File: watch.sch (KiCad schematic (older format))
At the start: 16 parts, among them IC1 ATMEGA48A-M

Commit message: Are finished yet? I think we are...
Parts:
- removed C? (x2): C, symbol C
- added C1, C2, C3, C4: C, symbol C
- added R1, R2, R3: R, symbol R
- gave numbers to parts that had none: 1
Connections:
- net labels added: LED01, LED02, LED03, LED04, LED05, LED06, LED07, LED08, LED09, LED10, LED11, LED12, MISO, MOSI, RESET, SCK, VCC
- wire segments 67 -> 109

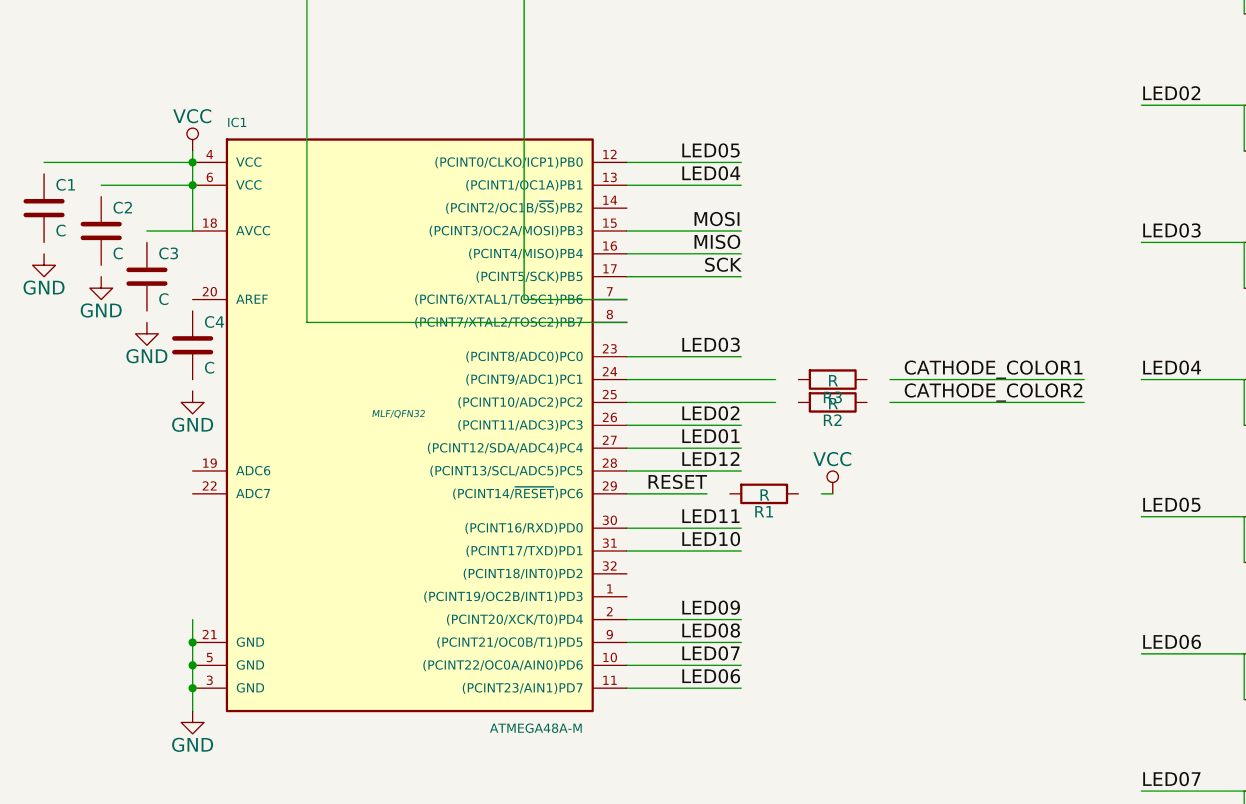
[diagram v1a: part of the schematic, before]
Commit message: Stupid kicad library update broke the schematics. Duhgit add .
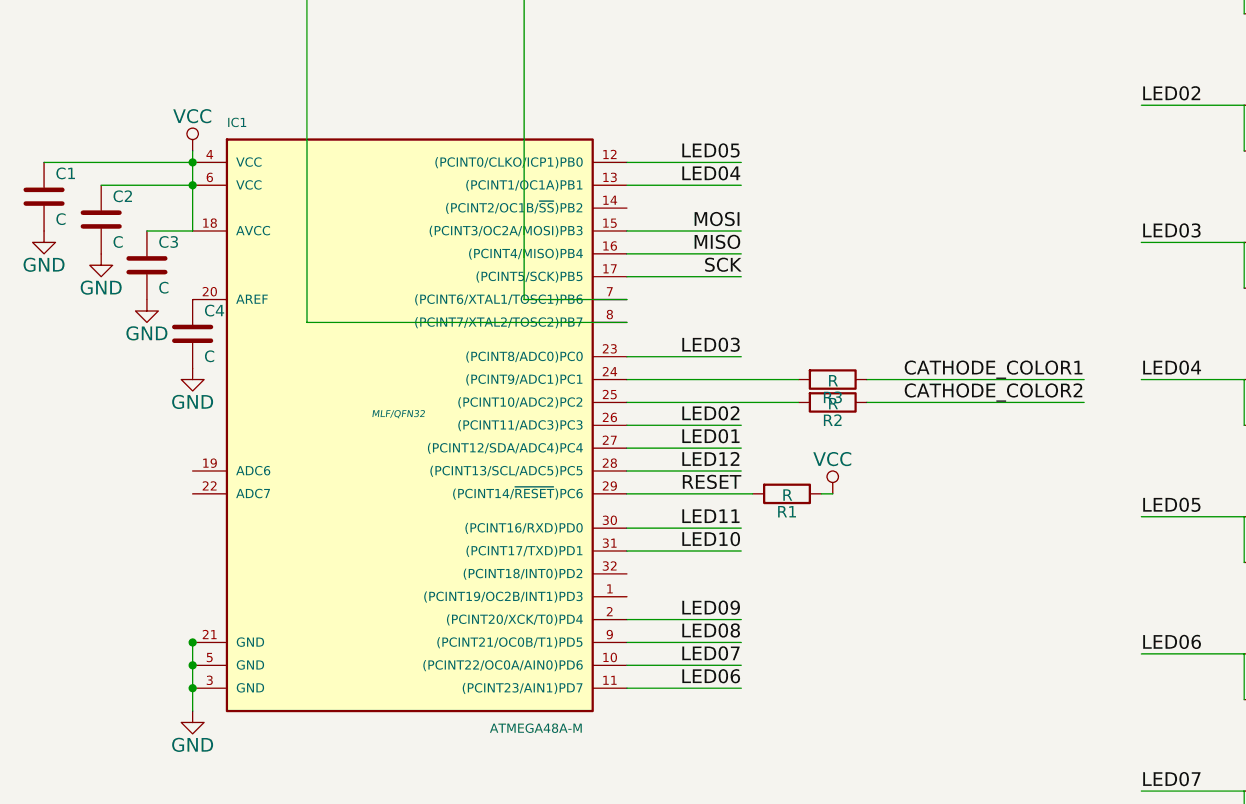
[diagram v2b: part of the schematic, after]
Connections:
- wire segments 109 -> 108
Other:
- moved on the sheet: C1, C2, C3, C4, R1
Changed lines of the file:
@@
 L R R1
 U 1 1 55044D46
-P 5650 3550
-F 0 "R1" V 5730 3550 50  0000 C CNN
-F 1 "R" V 5657 3551 50  0000 C CNN
-F 2 "" V 5580 3550 30  0000 C CNN
-F 3 "" H 5650 3550 30  0000 C CNN
-	1    5650 3550
+P 5750 3550
+F 0 "R1" V 5830 3550 50  0000 C CNN
+F 1 "R" V 5757 3551 50  0000 C CNN
+F 2 "" V 5680 3550 30  0000 C CNN
+F 3 "" H 5750 3550 30  0000 C CNN
+	1    5750 3550
 	0    1    1    0
 $EndComp
 Wire Wire Line
-	5400 3550 5050 3550
+	5600 3550 5050 3550
 $Comp
 L VCC #PWR01
@@
 L C C3
 U 1 1 550450EE
-P 2950 2600
-F 0 "C3" H 3000 2700 50  0000 L CNN
-F 1 "C" H 3000 2500 50  0000 L CNN
-F 2 "" H 2988 2450 30  0000 C CNN
-F 3 "" H 2950 2600 60  0000 C CNN
-	1    2950 2600
+P 2950 2550
+F 0 "C3" H 3000 2650 50  0000 L CNN
+F 1 "C" H 3000 2450 50  0000 L CNN
+F 2 "" H 2988 2400 30  0000 C CNN
+F 3 "" H 2950 2550 60  0000 C CNN
+	1    2950 2550
 	1    0    0    -1
 $EndComp
@@
 L C C2
 U 1 1 55045149
-P 2750 2400
-F 0 "C2" H 2800 2500 50  0000 L CNN
-F 1 "C" H 2800 2300 50  0000 L CNN
-F 2 "" H 2788 2250 30  0000 C CNN
-F 3 "" H 2750 2400 60  0000 C CNN
-	1    2750 2400
+P 2750 2350
+F 0 "C2" H 2800 2450 50  0000 L CNN
+F 1 "C" H 2800 2250 50  0000 L CNN
+F 2 "" H 2788 2200 30  0000 C CNN
+F 3 "" H 2750 2350 60  0000 C CNN
+	1    2750 2350
 	1    0    0    -1
 $EndComp
@@
 L C C1
 U 1 1 55045193
-P 2500 2300
-F 0 "C1" H 2550 2400 50  0000 L CNN
-F 1 "C" H 2550 2200 50  0000 L CNN
-F 2 "" H 2538 2150 30  0000 C CNN
-F 3 "" H 2500 2300 60  0000 C CNN
-	1    2500 2300
+P 2500 2250
+F 0 "C1" H 2550 2350 50  0000 L CNN
+F 1 "C" H 2550 2150 50  0000 L CNN
+F 2 "" H 2538 2100 30  0000 C CNN
+F 3 "" H 2500 2250 60  0000 C CNN
+	1    2500 2250
 	1    0    0    -1
 $EndComp
@@
 L C C4
 U 1 1 5504535B
-P 3150 2900
-F 0 "C4" H 3200 3000 50  0000 L CNN
-F 1 "C" H 3200 2800 50  0000 L CNN
-F 2 "" H 3188 2750 30  0000 C CNN
-F 3 "" H 3150 2900 60  0000 C CNN
-	1    3150 2900
+P 3150 2850
+F 0 "C4" H 3200 2950 50  0000 L CNN
+F 1 "C" H 3200 2750 50  0000 L CNN
+F 2 "" H 3188 2700 30  0000 C CNN
+F 3 "" H 3150 2850 60  0000 C CNN
+	1    3150 2850
 	1    0    0    -1
 $EndComp
@@
 L GND #PWR03
 U 1 1 55045394
-P 3150 3100
-F 0 "#PWR03" H 3150 2850 60  0001 C CNN
-F 1 "GND" H 3150 2950 60  0000 C CNN
-F 2 "" H 3150 3100 60  0000 C CNN
-F 3 "" H 3150 3100 60  0000 C CNN
-	1    3150 3100
+P 3150 3000
+F 0 "#PWR03" H 3150 2750 60  0001 C CNN
+F 1 "GND" H 3150 2850 60  0000 C CNN
+F 2 "" H 3150 3000 60  0000 C CNN
+F 3 "" H 3150 3000 60  0000 C CNN
+	1    3150 3000
 	1    0    0    -1
 $EndComp
@@
 L GND #PWR04
 U 1 1 550453D0
-P 2950 2800
-F 0 "#PWR04" H 2950 2550 60  0001 C CNN
-F 1 "GND" H 2950 2650 60  0000 C CNN
-F 2 "" H 2950 2800 60  0000 C CNN
-F 3 "" H 2950 2800 60  0000 C CNN
-	1    2950 2800
+P 2950 2700
+F 0 "#PWR04" H 2950 2450 60  0001 C CNN
+F 1 "GND" H 2950 2550 60  0000 C CNN
+F 2 "" H 2950 2700 60  0000 C CNN
+F 3 "" H 2950 2700 60  0000 C CNN
+	1    2950 2700
 	1    0    0    -1
 $EndComp
@@
 L GND #PWR05
 U 1 1 55045405
-P 2750 2600
-F 0 "#PWR05" H 2750 2350 60  0001 C CNN
-F 1 "GND" H 2750 2450 60  0000 C CNN
-F 2 "" H 2750 2600 60  0000 C CNN
-F 3 "" H 2750 2600 60  0000 C CNN
-	1    2750 2600
+P 2750 2500
+F 0 "#PWR05" H 2750 2250 60  0001 C CNN
+F 1 "GND" H 2750 2350 60  0000 C CNN
+F 2 "" H 2750 2500 60  0000 C CNN
+F 3 "" H 2750 2500 60  0000 C CNN
+	1    2750 2500
 	1    0    0    -1
 $EndComp
@@
 L GND #PWR06
 U 1 1 5504543A
-P 2500 2500
-F 0 "#PWR06" H 2500 2250 60  0001 C CNN
-F 1 "GND" H 2500 2350 60  0000 C CNN
-F 2 "" H 2500 2500 60  0000 C CNN
-F 3 "" H 2500 2500 60  0000 C CNN
-	1    2500 2500
+P 2500 2400
+F 0 "#PWR06" H 2500 2150 60  0001 C CNN
+F 1 "GND" H 2500 2250 60  0000 C CNN
+F 2 "" H 2500 2400 60  0000 C CNN
+F 3 "" H 2500 2400 60  0000 C CNN
+	1    2500 2400
 	1    0    0    -1
 $EndComp
@@
 $EndComp
 Wire Wire Line
-	3150 4100 3150 4200
-Wire Wire Line
 	3150 4200 3150 4300
 Wire Wire Line
@@
 Connection ~ 3150 4300
 Connection ~ 3150 4400
-Text Label 5400 3550 2    60   ~ 0
+Text Label 5550 3550 2    60   ~ 0
 RESET
 Wire Wire Line
@@
 Connection ~ 3150 4200
 Wire Wire Line
-	6200 3050 7050 3050
+	6100 3050 7050 3050
 Text Label 7050 3050 2    60   ~ 0
 CATHODE_COLOR1
 Wire Wire Line
-	6200 3150 7050 3150
+	6100 3150 7050 3150
 Text Label 7050 3150 2    60   ~ 0
 CATHODE_COLOR2
@@
 $EndComp
 Wire Wire Line
-	5700 3050 5050 3050
-Wire Wire Line
-	5700 3150 5050 3150
+	5800 3050 5050 3050
+Wire Wire Line
+	5800 3150 5050 3150
 $EndSCHEMATC
